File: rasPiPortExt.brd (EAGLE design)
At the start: 38 x 45 mm, 15 parts, among them IC1 MCP2300X/P, IC2 74LVC1G07DCK, IC3 74LVC1G07DCK, T1 BSS138PWWAVE, T2 BSS138PWWAVE, X3 SSW-103-02-S-T, X4 SSW-108-02-S-T

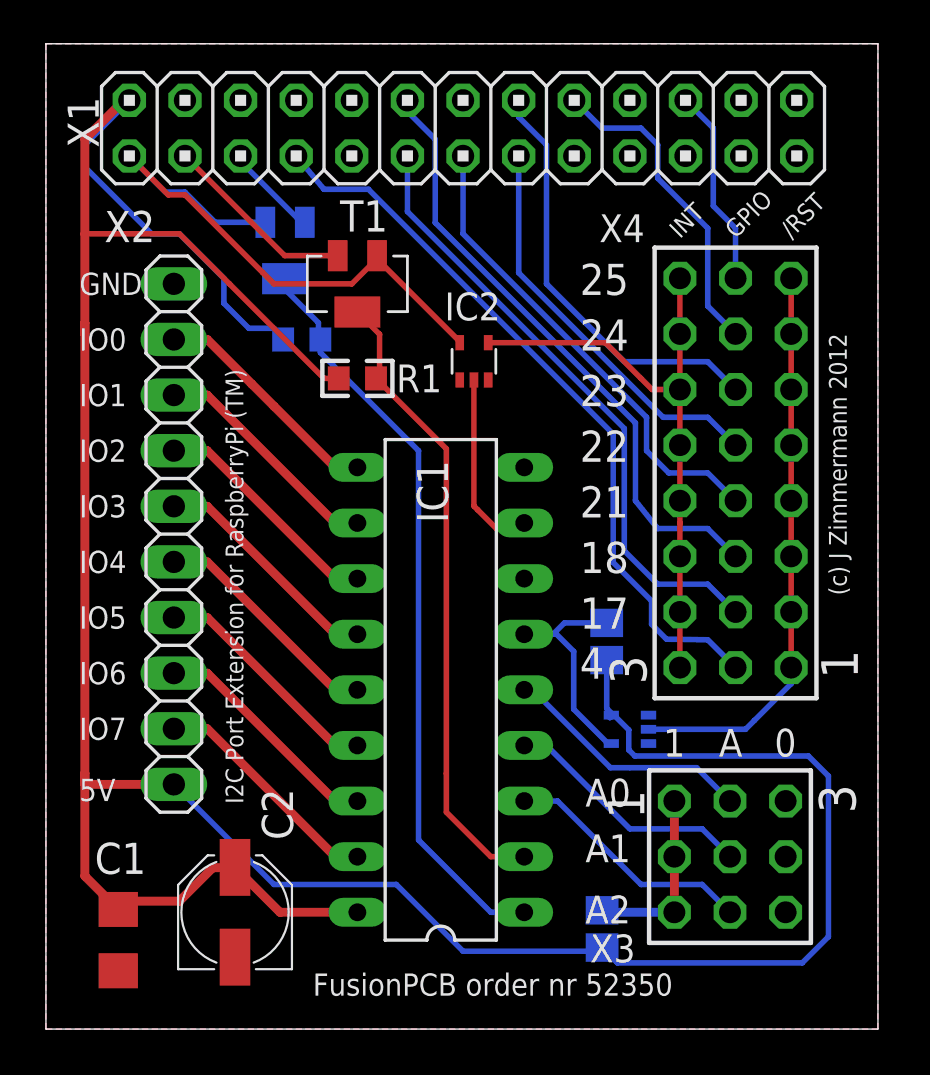
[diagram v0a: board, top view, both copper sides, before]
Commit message: changed design for /RST line, added additional R rearranged some components and traces v1.1 submitted for etching
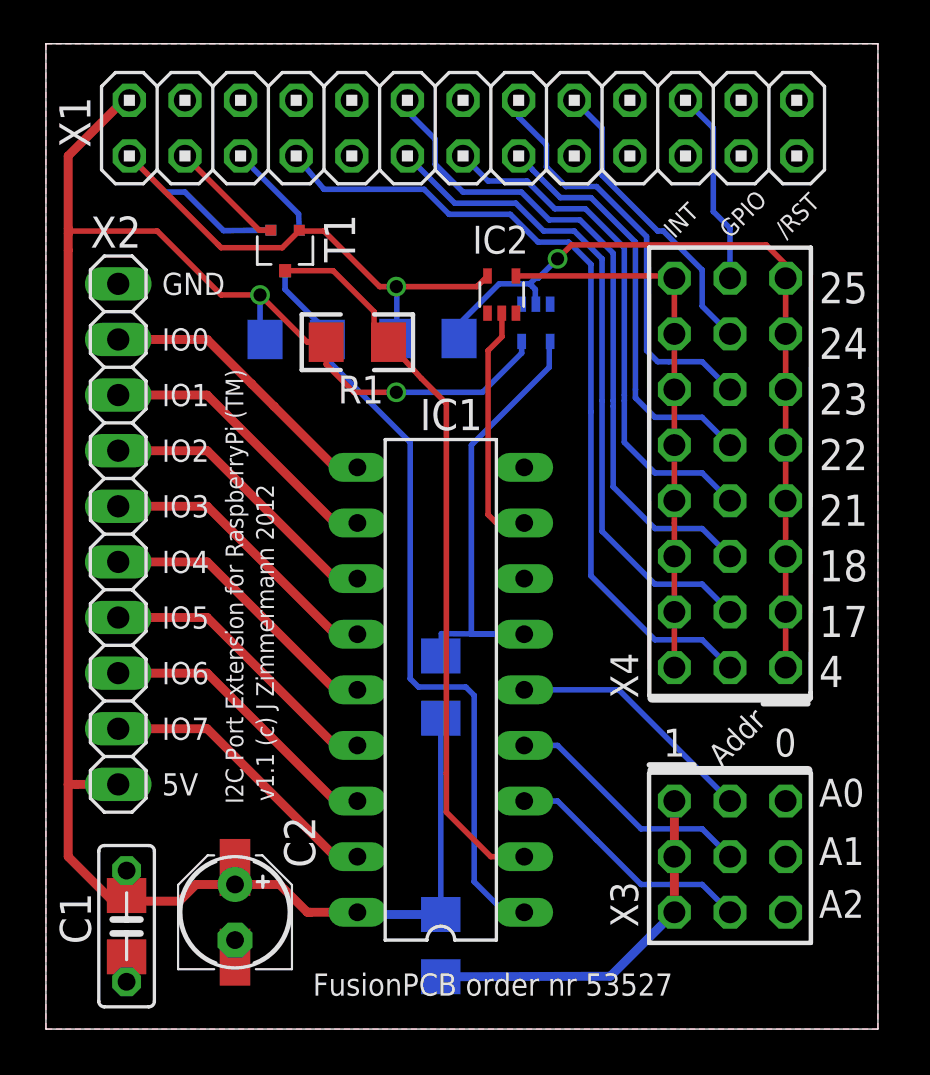
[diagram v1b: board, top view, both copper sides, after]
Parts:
- added C3: 100u, resistor:E2,5-5
- added C4: 100n, resistor:C050-025X075
- added R5: 10k, smdParts:R1206
- R1, R2: device smdParts:R0603 -> smdParts:R1206
- R3, R4: device smdParts:R0805 -> smdParts:R1206
- T1, T2: value BSS138PWWAVE -> BSS138PW"; device smdParts:SOT-323-WAVE -> smdParts:SOT-323
- X3: device con-samtec:SSW-103-02-S-T -> SD:SSW-103-02-S-T
- X4: value SSW-108-02-S-T -> (none); device con-samtec:SSW-108-02-S-T -> SD:SSW-108-02-S-T
- moved IC3 19.1 mm to (22.4, 32.3), turned to 180 degrees
- moved R4 16.1 mm to (17.4, 31.5), turned to 0 degrees
- moved R3 7.41 mm to (18.0, 3.81), turned to 90 degrees
- moved T1 3.64 mm to (10.9, 35.6)
- moved IC2 3.30 mm to (20.8, 33.5)
- moved X2 2.54 mm to (3.30, 22.6)
- moved R1 1.65 mm to (14.2, 31.4)
- moved C1 0.74 mm to (3.68, 4.70)
- moved R2 0.25 mm to (11.4, 31.5)
- moved X4 0.25 mm to (31.2, 25.4)
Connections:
- net +3V3: now also R4.2
- net +5V: now also C3.+, C4.1, R5.2; no longer R4.2
- net /RST: now also R5.1; no longer R4.1
- net GND: now also C3.-, C4.2
- net IO_/RST: now also R4.1
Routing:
- net +5V: track 144.9 -> 97.7 mm, vias 0 -> 2
- net /RST: track 10.3 -> 21.3 mm
- net IO_/RST: track 26.4 -> 37.4 mm, vias 0 -> 1
- net N$8: track 8.42 -> 17.0 mm
- net GPIO4: track 33.9 -> 37.9 mm
- net I2CB_SDA: track 29.8 -> 33.4 mm
- net I2C0_SDA: track 8.86 -> 5.33 mm
- net INT: track 8.59 -> 11.3 mm
- net N$11: track 10.8 -> 13.3 mm
- net N$9: track 10.8 -> 13.3 mm
- net N$7: track 10.8 -> 13.3 mm
- net N$6: track 10.8 -> 13.3 mm
- net N$5: track 10.8 -> 13.3 mm
- net N$4: track 10.8 -> 13.3 mm
- net N$12: track 10.8 -> 13.3 mm
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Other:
- board text added: "Addr"
- board text added: "Fit either IC3 and R4 or R5"
- board text added: "FusionPCB order nr 53527"
- board text added: "v1.1 (c) J Zimmermann 2012"
- board text removed: "(c) J Zimmermann 2012"
- board text removed: "A"
- board text removed: "FusionPCB order nr 52350"

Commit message: improved buffer for IRQ line, adding protection resistor
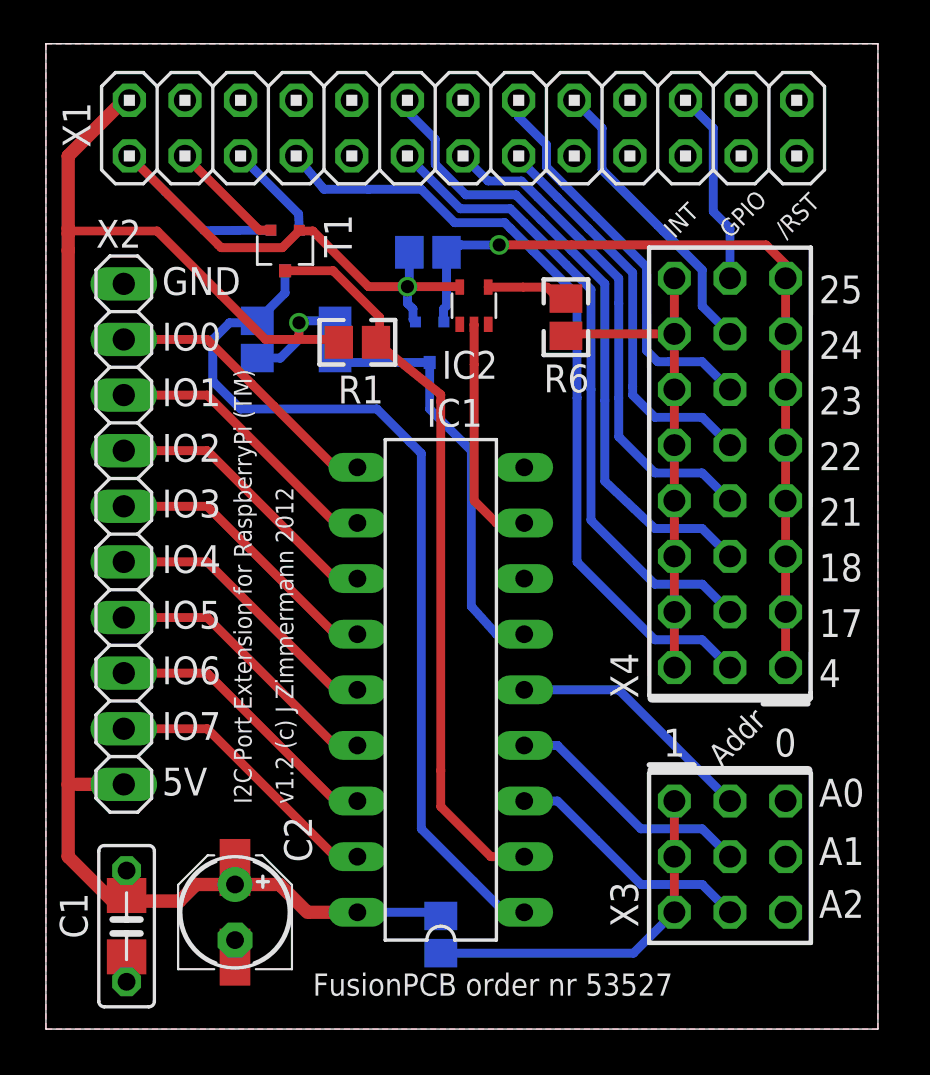
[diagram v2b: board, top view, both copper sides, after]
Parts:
- removed IC3: 74LVC1G07DCK, 74xx-little-us:SC70-5
- added R6: 1k, smdParts:R0805
- added T3: BSS138PW", smdParts:SOT-323
- R1, R2, R3, R4, R5: device smdParts:R1206 -> smdParts:R0805
- moved R5 16.6 mm to (13.2, 31.5), turned to 90 degrees
- moved R4 3.94 mm to (17.4, 35.5)
- moved R2 1.78 mm to (9.65, 31.5), turned to 90 degrees
- moved IC2 1.37 mm to (19.5, 33.0)
- moved R3 0.51 mm to (18.0, 4.32)
- moved X2 0.25 mm to (3.56, 22.6)
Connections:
- new net N$13: IC2.4, R6.1
- net +3V3: now also T3.P$1
- net +5V: no longer IC3.5
- net /RST: now also T3.P$3; no longer IC3.4
- net GND: no longer IC3.3
- net IO_/RST: now also T3.P$2; no longer IC3.2
- net IO_INT: now also R6.2; no longer IC2.4
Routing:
- net +5V: track 97.7 -> 81.3 mm, vias 2 -> 1
- net I2CB_SCL: track 36.0 -> 41.4 mm
- net N$13: track 0.00 -> 3.77 mm
- net IO_INT: track 25.1 -> 22.7 mm
- net /RST: track 21.3 -> 19.3 mm
- net GPIO4: track 37.9 -> 36.7 mm
- net GPIO17: track 30.6 -> 29.5 mm
- net GPIO18: track 30.6 -> 29.6 mm
- net GPIO21: track 23.9 -> 23.0 mm
- net GPIO22: track 19.3 -> 18.4 mm
- net IO_/RST: track 37.4 -> 38.3 mm
- net GPIO23: track 19.2 -> 18.4 mm
- net INT: track 11.3 -> 10.8 mm
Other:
- board text added: "v1.2 (c) J Zimmermann 2012"
- board text removed: "Fit either IC3 and R4 or R5"
- board text removed: "v1.1 (c) J Zimmermann 2012"

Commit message: added open source hardware logo
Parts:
- added U$1: (no value), ohw-logo:OSHW_FILLX70_NOTEXT
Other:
- board text added: "I2C Port Extension"
- board text added: "for RaspberryPi (TM)"
- board text removed: "FusionPCB order nr 53527"
- board text removed: "I2C Port Extension for RaspberryPi (TM)"
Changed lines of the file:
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@@
 <text x="35.306" y="30.607" size="1.27" layer="21" ratio="10">24</text>
 <text x="35.306" y="33.147" size="1.27" layer="21" ratio="10">25</text>
-<text x="9.398" y="10.287" size="0.8128" layer="21" rot="R90">I2C Port Extension for RaspberryPi (TM)</text>
-<text x="11.303" y="10.287" size="0.8128" layer="21" rot="R90">v1.2 (c) J Zimmermann 2012</text>
-<text x="12.192" y="1.524" size="1.016" layer="21">FusionPCB order nr 53527</text>
+<text x="12.192" y="2.667" size="0.8128" layer="21">I2C Port Extension</text>
+<text x="12.192" y="0.381" size="0.8128" layer="21">v1.2 (c) J Zimmermann 2012</text>
 <text x="5.3" y="10.668" size="1.27" layer="21">5V</text>
 <text x="5.3" y="30.988" size="1.27" layer="21">IO0</text>
@@
 <text x="28.194" y="12.446" size="1.27" layer="21" ratio="10">1</text>
 <text x="30.861" y="11.938" size="1.016" layer="21" rot="R45">Addr</text>
+<text x="12.192" y="1.524" size="0.8128" layer="21">for RaspberryPi (TM)</text>
 </plain>
 <attributes>
@@
 <attribute name="VALUE" x="21.082" y="35.433" size="1.27" layer="27" rot="R270"/>
 </element>
+<element name="U$1" library="ohw-logo" package="OSHW_FILLX70_NOTEXT" value="" x="34.925" y="0.889"/>
 </elements>
 <signals>
